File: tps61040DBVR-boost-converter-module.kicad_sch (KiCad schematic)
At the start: 0 parts

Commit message: Schematic Laid out
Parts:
- added C1, C3: 10uF, symbol Device:C
- added C2: 30pF, symbol Device:C
- added D1: ?, symbol Device:D_Schottky
- added L1: ?, symbol Device:L
- added R1, R2: ?, symbol Device:R
- added U1: TPS61040DBVR, DBV0005A, symbol TPS61040DBVR:TPS61040DBVR
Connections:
- new net +12V: C2.1, C3.1, D1.1 (K), R1.1
- new net +5V: C1.1, L1.1, U1.4 (EN), U1.5 (VIN)
- new net FB: C2.2, R1.2, R2.1, U1.3 (FB)
- new net GND: C1.2, C3.2, R2.2, U1.2 (GND)
- new net SW: D1.2 (A), L1.2, U1.1 (SW)

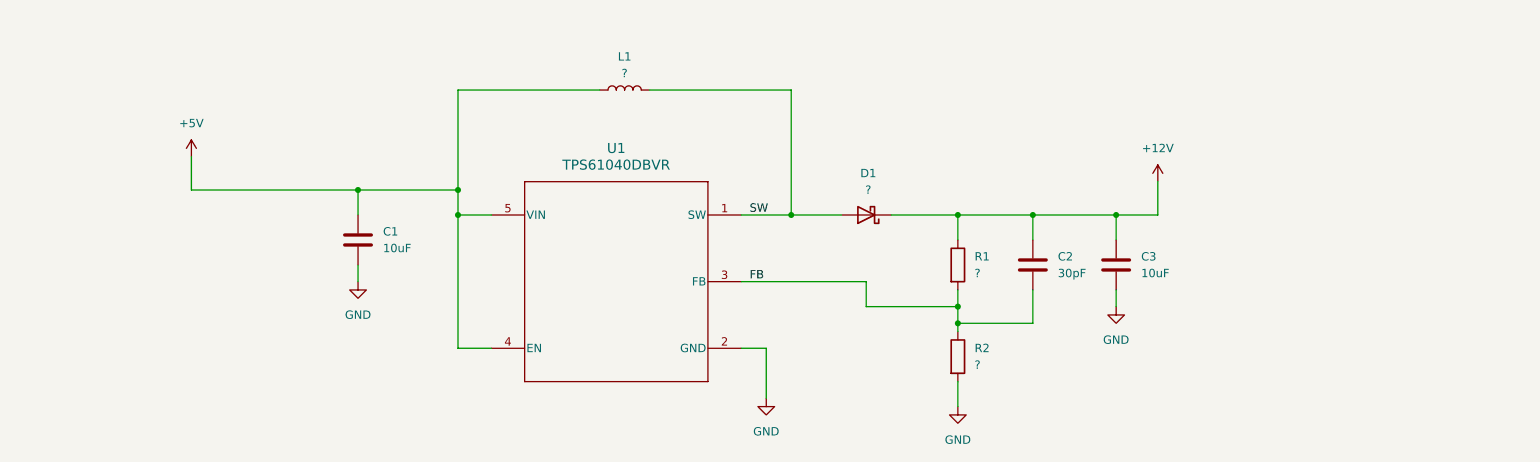
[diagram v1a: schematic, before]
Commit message: Assigned Footprints
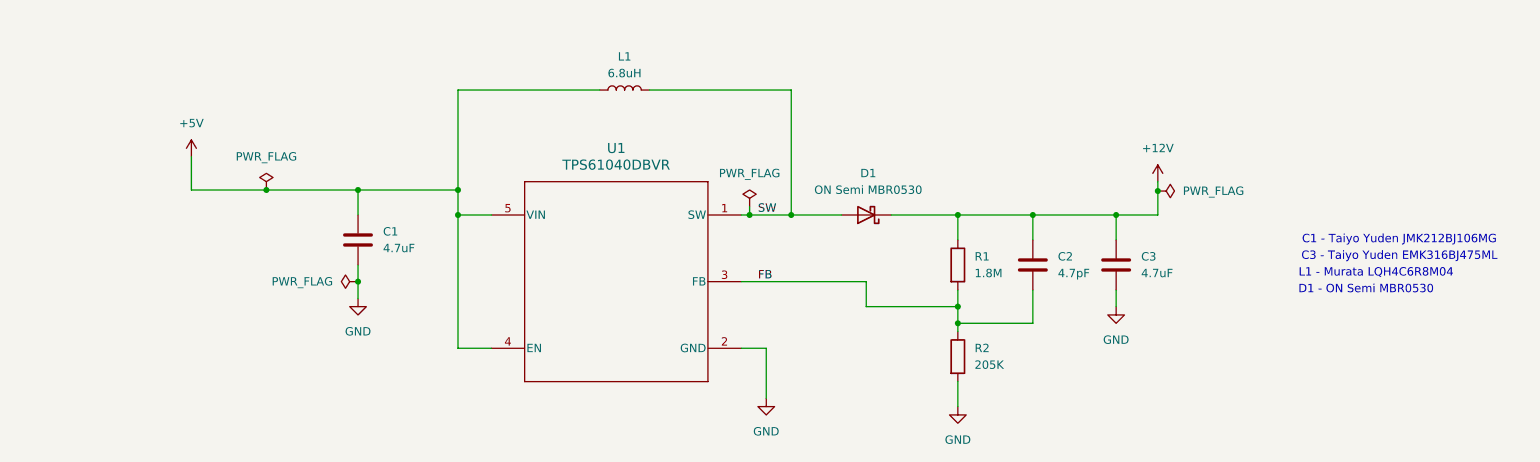
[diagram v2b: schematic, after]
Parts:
- C1, C3: value 10uF -> 4.7uF; footprint (none) -> Capacitor_SMD:C_1206_3216Metric_Pad1.33x1.80mm_HandSolder
- C2: value 30pF -> 4.7pF; footprint (none) -> Capacitor_SMD:C_0603_1608Metric_Pad1.08x0.95mm_HandSolder
- D1: value ? -> ON Semi MBR0530; footprint (none) -> Diode_SMD:D_SOD-123
- L1: value ? -> 6.8uH; footprint (none) -> Inductor_SMD:L_1812_4532Metric
- R1: value ? -> 1.8M; footprint (none) -> Resistor_SMD:R_0603_1608Metric_Pad0.98x0.95mm_HandSolder
- R2: value ? -> 205K; footprint (none) -> Resistor_SMD:R_0603_1608Metric_Pad0.98x0.95mm_HandSolder
- U1: footprint DBV0005A -> TPS61040DBVR:DBV0005A
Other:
- note added: "C1 - Taiyo Yuden JMK212BJ106MG"
- note added: "C3 - Taiyo Yuden EMK316BJ475ML"
- note added: "D1 - ON Semi MBR0530"
- note added: "L1 - Murata LQH4C6R8M04"

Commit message: Completed Routinf
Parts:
- added J1: +5V, Connector_PinHeader_1.00mm:PinHeader_1x01_P1.00mm_Vertical, symbol Connector:Conn_01x01_Pin
- added J2: +12V, Connector_PinHeader_1.00mm:PinHeader_1x01_P1.00mm_Vertical, symbol Connector:Conn_01x01_Pin
- added J3, J4: GND, Connector_PinHeader_1.00mm:PinHeader_1x01_P1.00mm_Vertical, symbol Connector:Conn_01x01_Pin
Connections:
- net +12V: now also J2.1 (Pin_1)
- net +5V: now also J1.1 (Pin_1)
- net GND: now also J3.1 (Pin_1), J4.1 (Pin_1)
